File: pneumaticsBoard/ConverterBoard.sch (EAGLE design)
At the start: 26 parts, among them IC1 MAX232, Q1 2N3819, Q2 2N3819, Q3 2N3819, Q4 2N3819, Q5 2N3819, Q6 2N3819, Q7 2N3819, Q8 2N3819, U1 ATMEGA328P-PU, X1 5566-4

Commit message: Added 12V-5V Con. Q needs attention. Layout changed to 1x6 rect.
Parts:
- removed X1: 5566-4, con-molex:5566-4
- added P1: 39-30-04_S, con-molex-mini-fit:39-30-04_S
- added U$1: CRL2S1205SC, CRL2S1205SC:CRL2S1205SC
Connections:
- removed net N$25: IC1G$1.R1IN, X1-2.S
- removed net N$26: IC1G$1.T1OUT, X1-3.S
- new net RX: IC1G$1.R1IN, P1-4.P
- new net TX: IC1G$1.T1OUT, P1-2.P
- new net VSS: CON1.2, CON2.2, CON3.2, CON4.2, CON5.2, CON6.2, CON7.2, CON8.2, P1-1.P, U$1.+VIN
- net GND: now also U$1.+VOUT; no longer CON1.2, CON2.2, CON3.2, CON4.2, CON5.2, CON6.2, CON7.2, CON8.2, X1-1.S
- net VCC: now also U$1.-VOUT
- net VDD: now also P1-3.P, U$1.-VIN; no longer X1-4.S

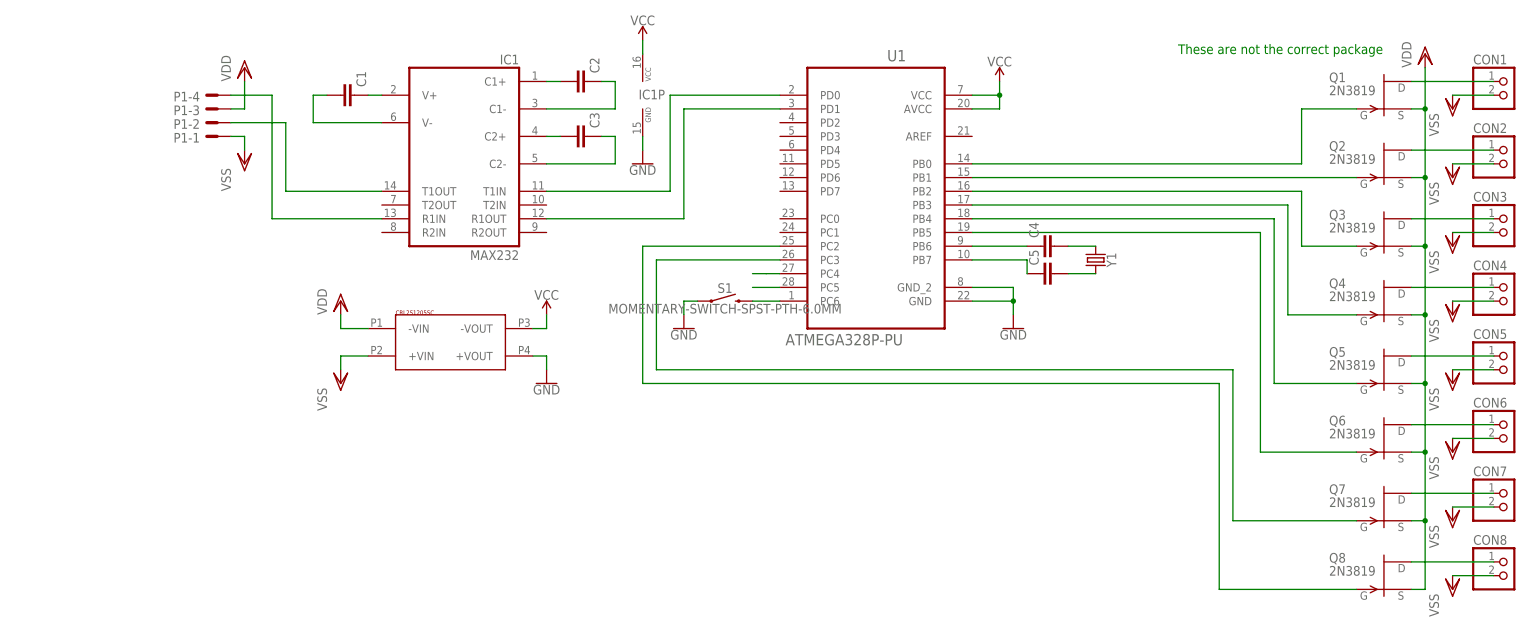
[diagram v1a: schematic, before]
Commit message: Pneumatics update - something incorrect with EAGLE GND planes
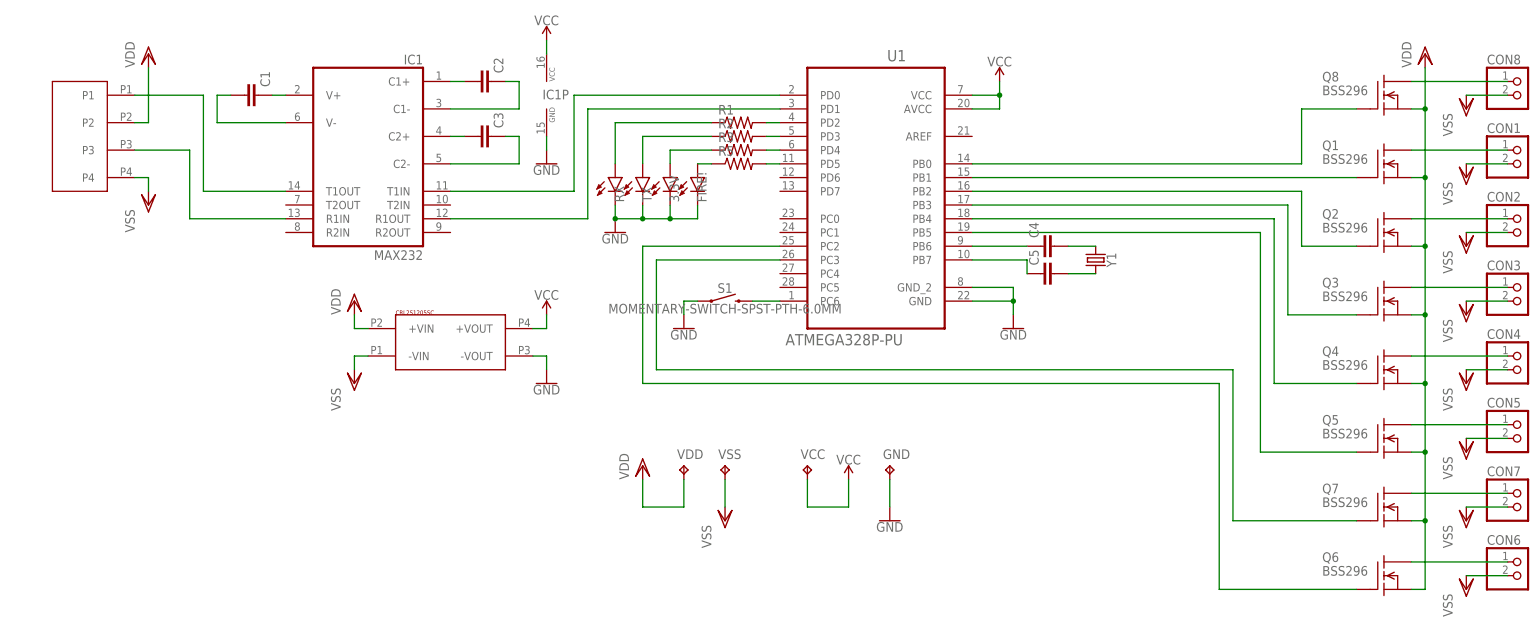
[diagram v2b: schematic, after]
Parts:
- removed P1: 39-30-04_S, con-molex-mini-fit:39-30-04_S
- added 3.3V, FIRE!, RX, TX: BLUE, SparkFun-LED:LED-BLUE0603
- added GND, VCC, VDD, VSS: TPTP11R, testpad:TPTP11R
- added R1, R2, R3, R5: (no value), resistor:R-US_0204/2V
- added U$2: MINI_FIT_JR_4PIN_VERT, 15-24-6041:MINI_FIT_JR_4PIN_VERT
- Q1, Q2, Q3, Q4, Q5, Q6, Q7, Q8: value 2N3819 -> BSS296; device transistor-fet:2N3819 -> transistor-fet:BSS296
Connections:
- net N$1 renamed Q7
- removed net N$3: Q2.G, U1.PB1
- removed net N$4: Q3.G, U1.PB2
- removed net N$5: Q4.G, U1.PB3
- removed net N$6: Q5.G, U1.PB4
- removed net SCL: U1.PC5
- removed net SDA: U1.PC4
- new net N$1: R3.2, U1.PD4
- new net N$25: R5.2, U1.PD5
- new net POWER: 3.3V.A, R3.1
- new net Q1: Q1.G, U1.PB1
- new net Q2: Q2.G, U1.PB2
- new net Q3: Q3.G, U1.PB3
- new net Q4: Q4.G, U1.PB4
- new net Q5: Q5.G, U1.PB5
- new net Q6: Q6.G, U1.PC2
- new net Q8: Q8.G, U1.PB0
- new net RX_ON: R1.1, RX.A
- new net TX_ON: R2.1, TX.A
- net GND: now also 3.3V.C, FIRE!.C, GND.TP, RX.C, TX.C, U$1.-VOUT; no longer U$1.+VOUT
- net N$2: now also FIRE!.A, R5.1; no longer Q1.G, U1.PB0
- net N$7: now also R1.2, U1.PD2; no longer Q6.G, U1.PB5
- net N$8: now also R2.2, U1.PD3; no longer Q8.G, U1.PC2
- net RX: now also U$2.P3; no longer P1-4.P
- net TX: now also U$2.P1; no longer P1-2.P
- net VCC: now also U$1.+VOUT, VCC.TP; no longer U$1.-VOUT
- net VDD: now also U$1.+VIN, U$2.P2, VDD.TP; no longer P1-3.P, U$1.-VIN
- net VSS: now also U$1.-VIN, U$2.P4, VSS.TP; no longer P1-1.P, U$1.+VIN
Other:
- note removed: "These are not the correct package"
- moved on the sheet: C1, C2, C3, CON1, CON2, CON3, CON4, CON5, CON6, CON7, CON8, IC1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

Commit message: Added Blaine's acoustics .sch - pneu almost done except for orphan adjustment
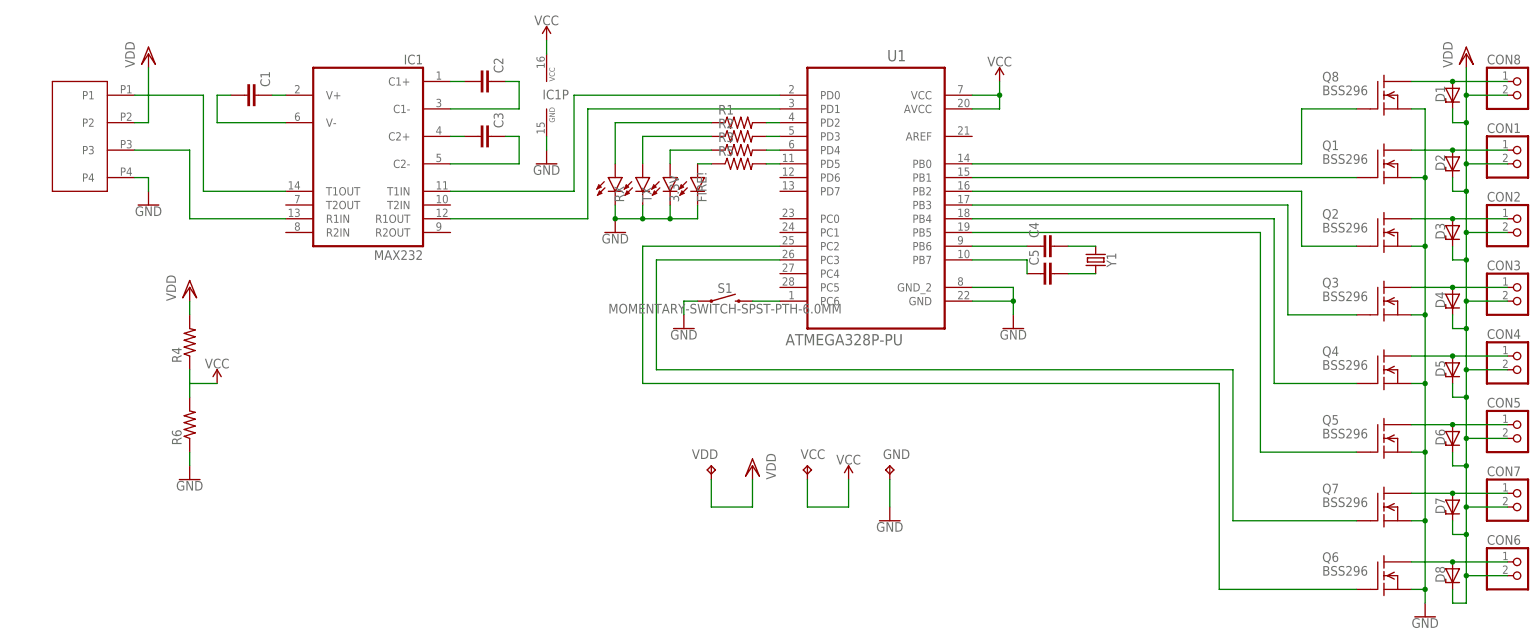
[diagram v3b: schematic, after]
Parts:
- removed U$1: CRL2S1205SC, CRL2S1205SC:CRL2S1205SC
- removed VSS: TPTP11R, testpad:TPTP11R
- added D1, D2, D3, D4, D5, D6, D7, D8: BZX90, diode:BZX90
- added R4, R6: (no value), resistor:R-US_0204/2V
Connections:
- removed net N$15: CON8.1, Q8.D
- removed net N$18: CON1.1, Q1.D
- removed net N$19: CON2.1, Q2.D
- removed net N$20: CON3.1, Q3.D
- removed net N$21: CON4.1, Q4.D
- removed net N$22: CON5.1, Q5.D
- removed net N$23: CON7.1, Q7.D
- removed net N$24: CON6.1, Q6.D
- removed net VSS: CON1.2, CON2.2, CON3.2, CON4.2, CON5.2, CON6.2, CON7.2, CON8.2, U$1.-VIN, U$2.P4, VSS.TP
- new net CON1_GND: CON1.1, D2.A, Q1.D
- new net CON2_GND: CON2.1, D3.A, Q2.D
- new net CON3_GND: CON3.1, D4.A, Q3.D
- new net CON4_GND: CON4.1, D5.A, Q4.D
- new net CON5_GND: CON5.1, D6.A, Q5.D
- new net CON6_GND: CON6.1, D8.A, Q6.D
- new net CON7_GND: CON7.1, D7.A, Q7.D
- new net CON8_GND: CON8.1, D1.A, Q8.D
- new net N$3: R4.1, R6.2
- net GND: now also Q1.S, Q2.S, Q3.S, Q4.S, Q5.S, Q6.S, Q7.S, Q8.S, R6.1, U$2.P4; no longer U$1.-VOUT
- net VCC: no longer U$1.+VOUT
- net VDD: now also CON1.2, CON2.2, CON3.2, CON4.2, CON5.2, CON6.2, CON7.2, CON8.2, D1.C, D2.C, D3.C, D4.C, D5.C, D6.C, D7.C, D8.C, R4.2; no longer Q1.S, Q2.S, Q3.S, Q4.S, Q5.S, Q6.S, Q7.S, Q8.S, U$1.+VIN
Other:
- moved on the sheet: VDD

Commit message: Finished Pneumatics Board, if RS232 still exists in a day
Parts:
- removed C2, C3, C4, C5: (no value), capacitor-wima:C2.5/2
- added C10, C8, C9: 1uF, SparkFun-Capacitors:470PF-0603-50V-5%
- added C6: 22pF, SparkFun-Capacitors:470PF-0603-50V-5%
- added PRESSURE: (no value), con-lstb:MA03-1
- C1: value (none) -> 22pF; device capacitor-wima:C2.5/2 -> SparkFun-Capacitors:470PF-0603-50V-5%
- R4: value (none) -> 4.7 K
- R6: value (none) -> 3.3 K
- Y1: value (none) -> 16 MHz
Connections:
- removed net N$16: C4.2, Y1.1
- removed net N$17: C5.2, Y1.2
- removed net N$25: R5.2, U1.PD5
- new net N$15: C1.2, Y1.1
- new net N$4: R5.2, U1.PC1
- new net N$5: C6.2, Y1.2
- new net N$6: PRESSURE.1, U1.PD5
- net GND: now also PRESSURE.3
- net N$10: now also C9.1; no longer C3.2
- net N$11: now also C8.2; no longer C2.1
- net N$12: now also C9.2; no longer C3.1
- net N$13: now also C10.2; no longer C1.1
- net N$14: now also C10.1; no longer C1.2
- net N$9: now also C8.1; no longer C2.2
- net Q1: now also U1.PC3; no longer U1.PB1
- net Q2: now also U1.PC2; no longer U1.PB2
- net Q3: now also U1.PB1; no longer U1.PB3
- net Q4: now also U1.PB2; no longer U1.PB4
- net Q5: now also U1.PB3; no longer U1.PB5
- net Q6: now also U1.PB4; no longer U1.PC2
- net Q7: now also U1.PB5; no longer U1.PC3
- net RS232_RX-ATMEGA_TX: now also U1.PD0; no longer U1.PD1
- net RS232_TX-ATMEGA_RX: now also U1.PD1; no longer U1.PD0
- net VCC: now also PRESSURE.2
- net XTAL1: now also C1.1; no longer C4.1
- net XTAL2: now also C6.1; no longer C5.1
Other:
- moved on the sheet: 3.3V, C1, FIRE!, IC1, IC1P, R1, R2, R3, R5, RX, TX, Y1
